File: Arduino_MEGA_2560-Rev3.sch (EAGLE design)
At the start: 63 parts, among them IC1 NCP1117ST50T3G, IC3 ATMEGA2560-16AU, IC4 ATMEGA16U2-MU, IC6 LP2985-33DBVR, IC7 LMV358IDGKR, T1 FDN340P, X1 POWERSUPPLY_DC21MMX, X2 USB-B_TH, Y1 CSTCE16M0V53-R0 16MHZ, Y2 16MHz

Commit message: Version inicial del Shield
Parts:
- removed C1, C14, C15: 22p, SmartPrj:C-EU0603-RND
- removed C10, C13: 1u, SmartPrj:C-EU0603-RND
- removed C11, C12, C2, C3, C4, C5, C6, C7, C8, C9: 100n, SmartPrj:C-EU0603-RND
- removed D1: M7, diode:DIODE-SMB
- removed D2, D3: CD1206-S01575, diode:DIODE-MINIMELF
- removed F1: MF-MSMF050-2 500mA, rcl:L-EUL1812
- removed FD1, FD2, FD3, FD4: FIDUCIALMOUNT, SmartPrj:FIDUCIALMOUNT
- removed GROUND, RESET-EN: (no value), jumper:SJ
- removed IC1: NCP1117ST50T3G, linear:MC33269ST-3.3T3
- removed IC3: ATMEGA2560-16AU, SmartPrj:ATMEGA25602560-16AU
- removed IC4: ATMEGA16U2-MU, SmartPrj:ATMEGA16U2-MU
- removed IC6: LP2985-33DBVR, SmartPrj:LP2985-XXDBVR33
- removed IC7: LMV358IDGKR, linear:LMV358MMX
- removed ICSP, ICSP1: 3x2M, SmartPrj:PINHD-2X3
- removed JP5: 2x2M - NM, SmartPrj:PINHD-2X2
- removed L, RX, TX: YELLOW, led:LEDCHIP-LED0805
- removed L1: BLM21, wuerth-elektronik:WE-CBF_0805
- removed ON: GREEN, led:LEDCHIP-LED0805
- removed PC1, PC2: 47u, rcl:CPOL-EUD
- removed RESET: TS42031-160R-TR-7260, SmartPrj:TS42
- removed RN1, RN5: 10K, resistor-dil:4R-NCAT16
- removed RN2: 22R, resistor-dil:4R-NCAY16
- removed RN3, RN4: 1k, resistor-dil:4R-NCAY16
- removed T1: FDN340P, zetex:PMOSSOT23
- removed X1: POWERSUPPLY_DC21MMX, SmartPrj:POWERSUPPLY_DC21MMX
- removed X2: USB-B_TH, SmartPrj:PN61729
- removed Y1: CSTCE16M0V53-R0 16MHZ, SmartPrj:RESONATORMU
- removed Y2: 16MHz, SmartPrj:XTAL/S
- removed Z1, Z2: CG0603MLC-05E, varistor:VARISTORCN0603
- added LED1, LED2: (no value), led:LEDCHIPLED_1206
- added R10, R11, R12, R13, R14, R15, R16, R17, R18, R19, R20, R3, R4, R5, R6, R7, R8, R9: (no value), resistor:R-EU_M1206
- added U$2, U$3, U$4, U$5, U$6, U$7, U$8, U$9: XPORT, SparkFun-Boards:XPORT
- R1, R2: value 1M -> (none); device SmartPrj:R-EU_R0603 -> resistor:R-EU_M1206
- U$1: value DISCLAIMER -> XPORT; device SmartPrj:DISCLAIMER -> SparkFun-Boards:XPORT
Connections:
- removed net 8PB4: IC4.(T1/PCINT4)PB4, JP5.1
- removed net 8PB5: IC4.(PCINT5)PB5, JP5.3
- removed net 8PB6: IC4.(PCINT6)PB6, JP5.2
- removed net 8PB7: IC4.(PCINT7/OC0A/OC1C)PB7, JP5.4
- removed net ADC0: ADCL.1, IC3.(ADC0)PF0
- removed net ADC1: ADCL.2, IC3.(ADC1)PF1
- removed net ADC10: ADCH.3, IC3.PK2(ADC10/PCINT18)
- removed net ADC11: ADCH.4, IC3.PK3(ADC11/PCINT19)
- removed net ADC12: ADCH.5, IC3.PK4(ADC12/PCINT20)
- removed net ADC13: ADCH.6, IC3.PK5(ADC13/PCINT21)
- removed net ADC14: ADCH.7, IC3.PK6(ADC14/PCINT22)
- removed net ADC15: ADCH.8, IC3.PK7(ADC15/PCINT23)
- removed net ADC2: ADCL.3, IC3.(ADC2)PF2
- removed net ADC3: ADCL.4, IC3.(ADC3)PF3
- removed net ADC4: ADCL.5, IC3.(ADC4/TCK)PF4
- removed net ADC5: ADCL.6, IC3.(ADC5/TMS)PF5
- removed net ADC6: ADCL.7, IC3.(ADC6/TDO)PF6
- removed net ADC7: ADCL.8, IC3.(ADC7/TDI)PF7
- removed net ADC8: ADCH.1, IC3.PK0(ADC8/PCINT16)
- removed net ADC9: ADCH.2, IC3.PK1(ADC9/PCINT17)
- removed net CMP: C12.2, IC7B.+IN, RN5C.1, RN5D.2
- removed net D+: RN2D.2, X2.3, Z2.2
- removed net D-: RN2A.2, X2.2, Z1.2
- removed net DTR: C7.1, IC4.(CTS/HWB/AIN6/TO/INT7)PD7, RN3D.1
- removed net GATE_CMD: IC7B.OUT, T1.G
- removed net L13: IC7A.-IN, IC7A.OUT, RN3B.2
- removed net M8RXD: IC4.(TXD1/INT3)PD3, RN4B.2
- removed net M8TXD: IC4.(RXD1/AIN1/INT2)PD2, RN4A.2
- removed net MISO2: IC4.(PD0/MISO/PCINT3)PB3, ICSP1.1
- removed net MOSI2: IC4.(PDI/MOSI/PCINT2)PB2, ICSP1.4
- removed net N$54: RN4D.1, RX.A
- removed net N$55: RN4C.1, TX.A
- removed net PWRIN: D1.A, X1.2
- removed net RD+: IC4.D+, RN2D.1
- removed net RD-: IC4.D-, RN2A.1
- removed net RESET2: D2.A, IC4.RESET(PC1/DW), ICSP1.5, RN5B.2
- removed net RXL: IC4.(INT5/AIN3)PD4, RX.C
- removed net SCK2: IC4.(SCLK/PCINT1)PB1, ICSP1.3
- removed net TXL: IC4.(XCK/AIN4/PCINT12)PD5, TX.C
- removed net UGND: C10.2, GROUND.1, IC4.UGND, L1.1, X2.4
- removed net USBVCC: C8.1, F1.1, IC4.UVCC, T1.D
- removed net USHIELD: L1.2, X2.P$1, X2.P$2, Z1.1, Z2.1
- removed net VUCAP: C10.1, IC4.UCAP
- removed net XT1: C14.1, IC4.XTAL1, R2.1, Y2.2
- removed net XT2: C15.1, IC4.XTAL2(PC0), R2.2, Y2.1
- removed net XTAL1: IC3.XTAL1, R1.1, Y1.3
- removed net XTAL2: IC3.XTAL2, R1.2, Y1.1
- removed net XVCC: F1.2, X2.1
- new net N$1: LED1.A, R1.1
- new net N$10: ADCH.3, R7.2
- new net N$11: ADCL.4, R14.2
- new net N$12: ADCL.5, R15.2
- new net N$13: ADCL.6, R16.2
- new net N$14: ADCL.7, R17.2
- new net N$15: ADCL.8, R18.2
- new net N$16: R12.1, U$8.DTR
- new net N$17: R13.1, U$8.RTS
- new net N$18: R14.1, U$8.RX
- new net N$19: R15.1, U$8.TX
- new net N$20: R16.1, U$8.RST
- new net N$21: ADCH.4, R8.2
- new net N$22: ADCH.5, R9.2
- new net N$23: ADCH.6, R10.2
- new net N$24: ADCH.7, R4.2
- new net N$25: ADCH.8, R3.2
- new net N$26: R17.1, U$2.CTS
- new net N$27: R18.1, U$2.DTR
- new net N$28: R5.1, U$2.RTS
- new net N$29: R6.1, U$2.RX
- new net N$30: R7.1, U$2.TX
- new net N$31: R8.1, U$2.RST
- new net N$32: R9.1, U$3.CTS
- new net N$33: R10.1, U$3.DTR
- new net N$34: R4.1, U$3.RTS
- new net N$35: R3.1, U$3.RX
- new net N$36: R19.1, U$3.RST
- new net N$37: R20.2, XIO.33
- new net N$4: ADCH.2, R6.2
- new net N$5: JP6.2
- new net N$6: R11.1, U$8.CTS
- new net N$7: ADCL.1, R11.2
- new net N$8: ADCL.2, R12.2
- new net N$9: ADCL.3, R13.2
- net +3V3: no longer C13.2, IC6.OUT, IC7B.-IN
- net +5V: now also R1.2, R2.2; no longer C11.2, C4.1, C5.1, C6.1, C9.1, D2.C, D3.C, IC1.OUT, IC1.OUT@1, IC3.AVCC, IC3.VCC, IC3.VCC1, IC3.VCC2, IC3.VCC3, IC4.AVCC, IC4.VCC, IC6.IN, IC6.ON/!OFF, IC7P.V+, ICSP.2, ICSP1.2, PC2.+, RN1B.2, RN1C.2, RN3A.1, RN4C.2, RN4D.2, RN5A.2, RN5B.1, T1.S
- net AREF: no longer C3.1, IC3.AREF
- net GND: now also LED1.C, LED2.C, U$1.3.3V, U$1.GND, U$2.3.3V, U$2.GND, U$3.3.3V, U$3.GND, U$4.3.3V, U$4.GND, U$5.3.3V, U$5.GND, U$6.3.3V, U$6.GND, U$7.3.3V, U$7.GND, U$8.3.3V, U$8.GND, U$9.3.3V, U$9.GND; no longer C1.2, C11.1, C12.1, C13.1, C14.2, C15.2, C2.2, C3.2, C4.2, C5.2, C6.2, C8.2, C9.2, GROUND.2, IC1.GND/ADJ, IC3.AGND, IC3.GND, IC3.GND1, IC3.GND2, IC3.GND3, IC4.GND, IC4.PAD, IC6.GND, IC7P.V-, ICSP.6, ICSP1.6, L.C, ON.C, PC1.-, PC2.-, RESET.1, RESET.2, RN3D.2, RN5D.1, X1.1, X1.3, Y1.2
- net N$2: now also LED2.A, R2.1; no longer L.A, RN3B.1
- net N$3: now also ADCH.1, R5.2; no longer ON.A, RN3A.2
- net PA0: no longer IC3.(AD0)PA0
- net PA1: no longer IC3.(AD1)PA1
- net PA2: no longer IC3.(AD2)PA2
- net PA3: no longer IC3.(AD3)PA3
- net PA4: no longer IC3.(AD4)PA4
- net PA5: no longer IC3.(AD5)PA5
- net PA6: no longer IC3.(AD6)PA6
- net PA7: no longer IC3.(AD7)PA7
- net PB0: now also R19.2; no longer IC3.(SS/PCINT0)PB0
- net PB1: now also R20.1, U$3.TX; no longer IC3.(SCK/PCINT1)PB1, ICSP.3, XIO.33
- net PB2: no longer IC3.(MOSI/PCINT2)PB2, ICSP.4
- net PB3: no longer IC3.(MISO/PCINT3)PB3, ICSP.1
- net PB4: no longer IC3.(OC2A/PCINT4)PB4
- net PB5: no longer IC3.(OC1A/PCINT5)PB5
- net PB6: no longer IC3.(OC1B/PCINT6)PB6
- net PB7: no longer IC3.(OC0A/OC1C/PCINT7)PB7, IC7A.+IN
- net PC0: no longer IC3.(A8)PC0
- net PC1: no longer IC3.(A9)PC1
- net PC2: no longer IC3.(A10)PC2
- net PC3: no longer IC3.(A11)PC3
- net PC4: no longer IC3.(A12)PC4
- net PC5: no longer IC3.(A13)PC5
- net PC6: no longer IC3.(A14)PC6
- net PC7: no longer IC3.(A15)PC7
- net PD7: no longer IC3.(T0)PD7
- net PE0: no longer IC3.(RXD0/PCIN8)PE0, RN4B.1
- net PE1: no longer IC3.(TXD0)PE1, RN4A.1
- net PE3: no longer IC3.(OC3A/AIN1)PE3
- net PE4: no longer IC3.(OC3B/INT4)PE4
- net PE5: no longer IC3.(OC3C/INT5)PE5
- net PG0: no longer IC3.(WR)PG0
- net PG1: no longer IC3.(RD)PG1
- net PG2: no longer IC3.(ALE)PG2
- net PG5: no longer IC3.(OC0B)PG5
- net PH3: no longer IC3.PH3(OC4A)
- net PH4: no longer IC3.PH4(OC4B)
- net PH5: no longer IC3.PH5(OC4C)
- net PH6: no longer IC3.PH6(OC2B)
- net PL0: no longer IC3.PL0(ICP4)
- net PL1: no longer IC3.PL1(ICP5)
- net PL2: no longer IC3.PL2(T5)
- net PL3: no longer IC3.PL3(OC5A)
- net PL4: no longer IC3.PL4(OC5B)
- net PL5: no longer IC3.PL5(OC5C)
- net PL6: no longer IC3.PL6
- net PL7: no longer IC3.PL7
- net RESET: no longer C1.1, C7.2, D3.A, IC3.RESET, ICSP.5, RESET-EN.1, RESET-EN.2, RESET.3, RESET.4, RN5A.1
- net RXD1: no longer IC3.(RXD1/INT2)PD2
- net RXD2: no longer IC3.PH0(RXD2)
- net RXD3: no longer IC3.PJ0(RXD3/PCINT9)
- net SCL: no longer IC3.(SCL/INT0)PD0, RN1B.1
- net SDA: no longer IC3.(SDA/INT1)PD1, JP6.2, RN1C.1
- net TXD1: no longer IC3.(TXD1/INT3)PD3
- net TXD2: no longer IC3.PH1(TXD2)
- net TXD3: no longer IC3.PJ1(TXD3/PCINT10)
- net VIN: no longer C2.1, D1.C, IC1.IN, PC1.+, RN5C.2
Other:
- note removed: "USB boot En"
- moved on the sheet: ADCH, ADCL, COMMUNICATION, JP6, PWML, R1, R2, XIO

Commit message: nuevas dimensiones placa
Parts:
- removed R10, R16, R17, R18, R4, R5, R6, R9: (no value), resistor:R-EU_M1206
- added R21, R25: (no value), rcl:R-US_0207/2V
- R11, R12, R13, R14, R15, R19, R20, R3, R7, R8: device resistor:R-EU_M1206 -> rcl:R-US_0207/10
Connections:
- removed net N$18: R14.1, U$8.RX
- removed net N$19: R15.1, U$8.TX
- removed net N$20: R16.1, U$8.RST
- removed net N$26: R17.1, U$2.CTS
- removed net N$27: R18.1, U$2.DTR
- removed net N$28: R5.1, U$2.RTS
- removed net N$29: R6.1, U$2.RX
- removed net N$32: R9.1, U$3.CTS
- removed net N$33: R10.1, U$3.DTR
- removed net N$34: R4.1, U$3.RTS
- removed net N$35: R3.1, U$3.RX
- new net N$38: R21.2, U$7.TX
- new net N$39: R25.1, U$7.RST
- new net N$44: R11.1, U$8.RST
- new net N$45: R12.1, U$8.TX
- new net N$46: R13.2, U$8.3.3V, U$8.GND
- net GND: now also R13.1, R14.2, R15.1, R3.2; no longer U$2.3.3V, U$2.GND, U$3.3.3V, U$3.GND, U$7.3.3V, U$7.GND, U$8.3.3V, U$8.GND
- net N$11: now also U$8.RX; no longer R14.2
- net N$12: now also R12.2; no longer R15.2
- net N$13: now also R11.2; no longer R16.2
- net N$14: now also U$2.CTS; no longer R17.2
- net N$15: now also U$2.DTR; no longer R18.2
- net N$16: now also R15.2, U$2.3.3V, U$2.GND; no longer R12.1, U$8.DTR
- net N$17: now also R3.1, U$3.3.3V, U$3.GND; no longer R13.1, U$8.RTS
- net N$22: now also U$3.CTS; no longer R9.2
- net N$23: now also U$3.DTR; no longer R10.2
- net N$24: now also U$3.RTS; no longer R4.2
- net N$25: now also U$3.RX; no longer R3.2
- net N$3: now also U$2.RTS; no longer R5.2
- net N$4: now also U$2.RX; no longer R6.2
- net N$6: now also R14.1, U$7.3.3V, U$7.GND; no longer R11.1, U$8.CTS
- net N$7: now also U$8.CTS; no longer R11.2
- net N$8: now also U$8.DTR; no longer R12.2
- net N$9: now also U$8.RTS; no longer R13.2
- net PB2: now also U$1.DTR
- net PB3: now also U$1.CTS
- net PB4: now also U$7.CTS
- net PB5: now also R21.1
- net PB6: now also R25.2
- net PB7: now also U$7.RX
- net PG0: now also U$9.RST
- net PG1: now also U$9.TX
- net PH5: now also U$7.DTR
- net PH6: now also U$7.RTS
- net PL0: now also U$1.RX
- net PL1: now also U$1.RTS
- net PL2: now also U$1.RST
- net PL3: now also U$1.TX
- net PL4: now also U$9.DTR
- net PL5: now also U$9.CTS
- net PL6: now also U$9.RX
- net PL7: now also U$9.RTS
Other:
- moved on the sheet: U$1, U$4, U$5, U$6, U$7, U$9

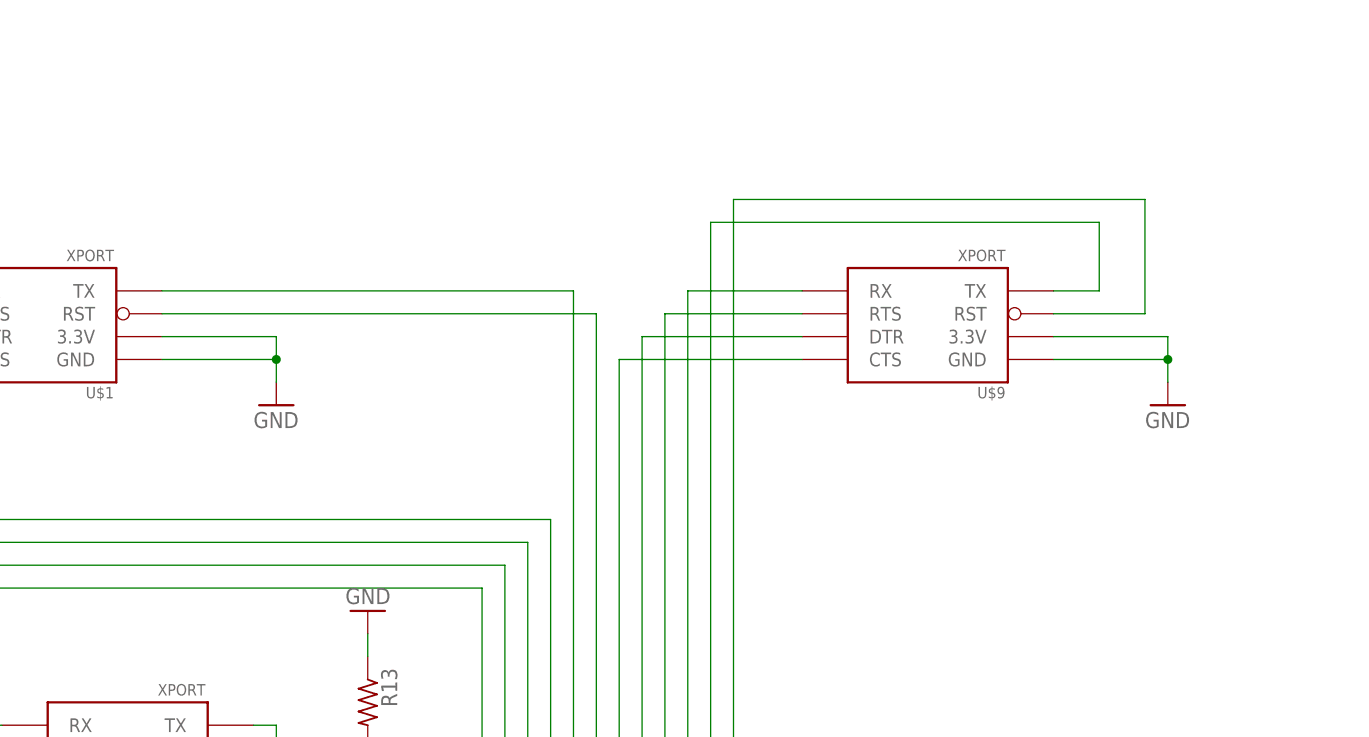
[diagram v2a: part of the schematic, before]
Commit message: nuevas resistencias, revisar los pines de entrada salida
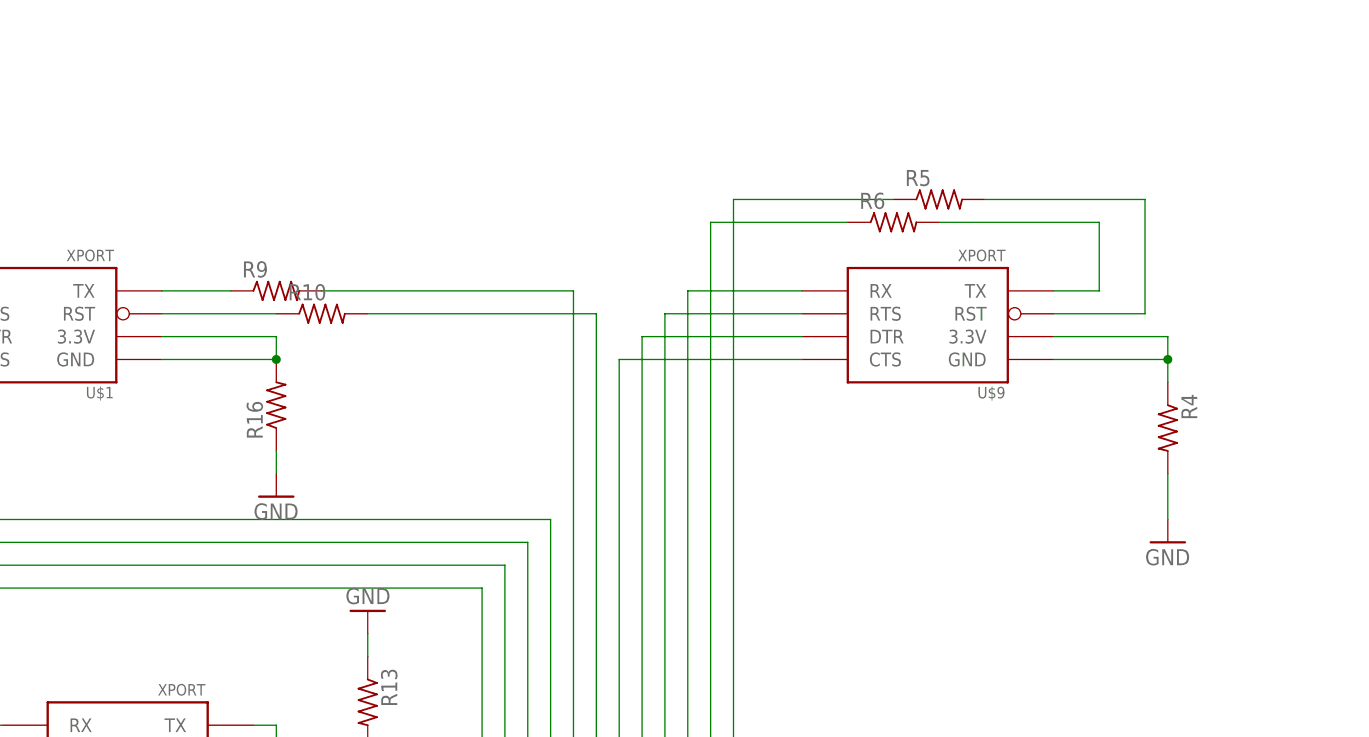
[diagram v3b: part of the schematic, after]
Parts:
- added R10, R16, R4, R5, R6, R9: (no value), rcl:R-US_0207/15
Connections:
- new net N$18: R4.1, U$9.3.3V, U$9.GND
- new net N$19: R5.2, U$9.RST
- new net N$20: R6.2, U$9.TX
- new net N$26: R16.2, U$1.3.3V, U$1.GND
- new net N$27: R10.1, U$1.RST
- new net N$28: R9.1, U$1.TX
- net GND: now also R16.1, R4.2; no longer U$1.3.3V, U$1.GND, U$9.3.3V, U$9.GND
- net PG0: now also R5.1; no longer U$9.RST
- net PG1: now also R6.1; no longer U$9.TX
- net PL2: now also R10.2; no longer U$1.RST
- net PL3: now also R9.2; no longer U$1.TX
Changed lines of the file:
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@@
 <part name="R15" library="rcl" deviceset="R-US_" device="0207/10"/>
 <part name="R3" library="rcl" deviceset="R-US_" device="0207/10"/>
+<part name="R4" library="rcl" deviceset="R-US_" device="0207/15"/>
+<part name="R5" library="rcl" deviceset="R-US_" device="0207/15"/>
+<part name="R6" library="rcl" deviceset="R-US_" device="0207/15"/>
+<part name="R9" library="rcl" deviceset="R-US_" device="0207/15"/>
+<part name="R10" library="rcl" deviceset="R-US_" device="0207/15"/>
+<part name="R16" library="rcl" deviceset="R-US_" device="0207/15"/>
 </parts>
 <sheets>
@@
 <attribute name="VALUE" x="230.886" y="146.812" size="1.27" layer="96" rot="R180"/>
 </instance>
-<instance part="GND1" gate="1" x="149.86" y="129.54" smashed="yes">
-<attribute name="VALUE" x="147.32" y="127" size="1.778" layer="96"/>
+<instance part="GND1" gate="1" x="149.86" y="119.38" smashed="yes">
+<attribute name="VALUE" x="147.32" y="116.84" size="1.778" layer="96"/>
 </instance>
 <instance part="GND2" gate="1" x="350.52" y="185.42" smashed="yes" rot="R180">
@@
 <attribute name="VALUE" x="162.56" y="109.22" size="1.778" layer="96" rot="R180"/>
 </instance>
-<instance part="GND14" gate="1" x="248.92" y="129.54" smashed="yes">
-<attribute name="VALUE" x="246.38" y="127" size="1.778" layer="96"/>
+<instance part="GND14" gate="1" x="248.92" y="114.3" smashed="yes">
+<attribute name="VALUE" x="246.38" y="111.76" size="1.778" layer="96"/>
 </instance>
 <instance part="R7" gate="G$1" x="83.82" y="50.8" smashed="yes" rot="R180">
@@
 <attribute name="NAME" x="151.3586" y="29.21" size="1.778" layer="95" rot="R270"/>
 <attribute name="VALUE" x="146.558" y="29.21" size="1.778" layer="96" rot="R270"/>
+</instance>
+<instance part="R4" gate="G$1" x="248.92" y="127" smashed="yes" rot="R270">
+<attribute name="NAME" x="250.4186" y="130.81" size="1.778" layer="95" rot="R270"/>
+<attribute name="VALUE" x="245.618" y="130.81" size="1.778" layer="96" rot="R270"/>
+</instance>
+<instance part="R5" gate="G$1" x="223.52" y="152.4" smashed="yes">
+<attribute name="NAME" x="219.71" y="153.8986" size="1.778" layer="95"/>
+<attribute name="VALUE" x="219.71" y="149.098" size="1.778" layer="96"/>
+</instance>
+<instance part="R6" gate="G$1" x="218.44" y="149.86" smashed="yes">
+<attribute name="NAME" x="214.63" y="151.3586" size="1.778" layer="95"/>
+<attribute name="VALUE" x="214.63" y="146.558" size="1.778" layer="96"/>
+</instance>
+<instance part="R9" gate="G$1" x="149.86" y="142.24" smashed="yes">
+<attribute name="NAME" x="146.05" y="143.7386" size="1.778" layer="95"/>
+<attribute name="VALUE" x="146.05" y="138.938" size="1.778" layer="96"/>
+</instance>
+<instance part="R10" gate="G$1" x="154.94" y="139.7" smashed="yes">
+<attribute name="NAME" x="151.13" y="141.1986" size="1.778" layer="95"/>
+<attribute name="VALUE" x="151.13" y="136.398" size="1.778" layer="96"/>
+</instance>
+<instance part="R16" gate="G$1" x="149.86" y="129.54" smashed="yes" rot="R90">
+<attribute name="NAME" x="148.3614" y="125.73" size="1.778" layer="95" rot="R90"/>
+<attribute name="VALUE" x="153.162" y="125.73" size="1.778" layer="96" rot="R90"/>
 </instance>
 </instances>
@@
 </segment>
 <segment>
-<pinref part="GND1" gate="1" pin="GND"/>
-<pinref part="U$1" gate="G$1" pin="GND"/>
-<wire x1="137.16" y1="134.62" x2="149.86" y2="134.62" width="0.1524" layer="91"/>
-<wire x1="149.86" y1="134.62" x2="149.86" y2="132.08" width="0.1524" layer="91"/>
-<junction x="149.86" y="134.62"/>
-<wire x1="149.86" y1="137.16" x2="149.86" y2="134.62" width="0.1524" layer="91"/>
-<pinref part="U$1" gate="G$1" pin="3.3V"/>
-<wire x1="137.16" y1="137.16" x2="149.86" y2="137.16" width="0.1524" layer="91"/>
-</segment>
-<segment>
 <pinref part="LED1" gate="G$1" pin="C"/>
 <pinref part="GND3" gate="1" pin="GND"/>
@@
 </segment>
 <segment>
-<pinref part="U$9" gate="G$1" pin="GND"/>
-<wire x1="236.22" y1="134.62" x2="248.92" y2="134.62" width="0.1524" layer="91"/>
-<pinref part="U$9" gate="G$1" pin="3.3V"/>
-<wire x1="236.22" y1="137.16" x2="248.92" y2="137.16" width="0.1524" layer="91"/>
-<wire x1="248.92" y1="137.16" x2="248.92" y2="134.62" width="0.1524" layer="91"/>
-<pinref part="GND14" gate="1" pin="GND"/>
-<wire x1="248.92" y1="132.08" x2="248.92" y2="134.62" width="0.1524" layer="91"/>
-<junction x="248.92" y="134.62"/>
-</segment>
-<segment>
 <pinref part="U$6" gate="G$1" pin="GND"/>
 <wire x1="495.3" y1="152.4" x2="482.6" y2="152.4" width="0.1524" layer="91"/>
@@
 <pinref part="GND7" gate="1" pin="GND"/>
 <wire x1="149.86" y1="20.32" x2="149.86" y2="17.78" width="0.1524" layer="91"/>
+</segment>
+<segment>
+<pinref part="R4" gate="G$1" pin="2"/>
+<pinref part="GND14" gate="1" pin="GND"/>
+<wire x1="248.92" y1="121.92" x2="248.92" y2="116.84" width="0.1524" layer="91"/>
+</segment>
+<segment>
+<pinref part="GND1" gate="1" pin="GND"/>
+<pinref part="R16" gate="G$1" pin="1"/>
+<wire x1="149.86" y1="121.92" x2="149.86" y2="124.46" width="0.1524" layer="91"/>
 </segment>
 </net>
@@
 <wire x1="248.92" y1="58.42" x2="200.66" y2="58.42" width="0.1524" layer="91"/>
 <wire x1="200.66" y1="58.42" x2="200.66" y2="152.4" width="0.1524" layer="91"/>
-<wire x1="200.66" y1="152.4" x2="246.38" y2="152.4" width="0.1524" layer="91"/>
-<wire x1="246.38" y1="152.4" x2="246.38" y2="139.7" width="0.1524" layer="91"/>
-<pinref part="U$9" gate="G$1" pin="RST"/>
-<wire x1="246.38" y1="139.7" x2="236.22" y2="139.7" width="0.1524" layer="91"/>
+<pinref part="R5" gate="G$1" pin="1"/>
+<wire x1="200.66" y1="152.4" x2="218.44" y2="152.4" width="0.1524" layer="91"/>
 </segment>
 <segment>
@@
 <wire x1="185.42" y1="55.88" x2="198.12" y2="55.88" width="0.1524" layer="91"/>
 <wire x1="198.12" y1="55.88" x2="198.12" y2="149.86" width="0.1524" layer="91"/>
-<wire x1="198.12" y1="149.86" x2="241.3" y2="149.86" width="0.1524" layer="91"/>
-<wire x1="241.3" y1="149.86" x2="241.3" y2="142.24" width="0.1524" layer="91"/>
-<pinref part="U$9" gate="G$1" pin="TX"/>
-<wire x1="241.3" y1="142.24" x2="236.22" y2="142.24" width="0.1524" layer="91"/>
+<pinref part="R6" gate="G$1" pin="1"/>
+<wire x1="198.12" y1="149.86" x2="213.36" y2="149.86" width="0.1524" layer="91"/>
 </segment>
 <segment>
@@
 <wire x1="256.54" y1="71.12" x2="185.42" y2="71.12" width="0.1524" layer="91"/>
 <wire x1="185.42" y1="71.12" x2="185.42" y2="139.7" width="0.1524" layer="91"/>
-<pinref part="U$1" gate="G$1" pin="RST"/>
-<wire x1="185.42" y1="139.7" x2="137.16" y2="139.7" width="0.1524" layer="91"/>
+<pinref part="R10" gate="G$1" pin="2"/>
+<wire x1="160.02" y1="139.7" x2="185.42" y2="139.7" width="0.1524" layer="91"/>
 </segment>
 </net>
@@
 <wire x1="177.8" y1="63.5" x2="182.88" y2="63.5" width="0.1524" layer="91"/>
 <wire x1="182.88" y1="63.5" x2="182.88" y2="142.24" width="0.1524" layer="91"/>
-<pinref part="U$1" gate="G$1" pin="TX"/>
-<wire x1="182.88" y1="142.24" x2="137.16" y2="142.24" width="0.1524" layer="91"/>
+<pinref part="R9" gate="G$1" pin="2"/>
+<wire x1="154.94" y1="142.24" x2="182.88" y2="142.24" width="0.1524" layer="91"/>
 </segment>
 </net>
@@
 </segment>
 </net>
+<net name="N$18" class="2">
+<segment>
+<pinref part="U$9" gate="G$1" pin="GND"/>
+<wire x1="236.22" y1="134.62" x2="248.92" y2="134.62" width="0.1524" layer="91"/>
+<pinref part="U$9" gate="G$1" pin="3.3V"/>
+<wire x1="236.22" y1="137.16" x2="248.92" y2="137.16" width="0.1524" layer="91"/>
+<wire x1="248.92" y1="137.16" x2="248.92" y2="134.62" width="0.1524" layer="91"/>
+<pinref part="R4" gate="G$1" pin="1"/>
+<wire x1="248.92" y1="132.08" x2="248.92" y2="134.62" width="0.1524" layer="91"/>
+<junction x="248.92" y="134.62"/>
+</segment>
+</net>
+<net name="N$19" class="0">
+<segment>
+<pinref part="U$9" gate="G$1" pin="RST"/>
+<wire x1="246.38" y1="152.4" x2="246.38" y2="139.7" width="0.1524" layer="91"/>
+<wire x1="246.38" y1="139.7" x2="236.22" y2="139.7" width="0.1524" layer="91"/>
+<pinref part="R5" gate="G$1" pin="2"/>
+<wire x1="228.6" y1="152.4" x2="246.38" y2="152.4" width="0.1524" layer="91"/>
+</segment>
+</net>
+<net name="N$20" class="0">
+<segment>
+<pinref part="U$9" gate="G$1" pin="TX"/>
+<wire x1="241.3" y1="149.86" x2="241.3" y2="142.24" width="0.1524" layer="91"/>
+<wire x1="241.3" y1="142.24" x2="236.22" y2="142.24" width="0.1524" layer="91"/>
+<pinref part="R6" gate="G$1" pin="2"/>
+<wire x1="223.52" y1="149.86" x2="241.3" y2="149.86" width="0.1524" layer="91"/>
+</segment>
+</net>
+<net name="N$26" class="2">
+<segment>
+<pinref part="U$1" gate="G$1" pin="GND"/>
+<wire x1="137.16" y1="134.62" x2="149.86" y2="134.62" width="0.1524" layer="91"/>
+<wire x1="149.86" y1="137.16" x2="149.86" y2="134.62" width="0.1524" layer="91"/>
+<pinref part="U$1" gate="G$1" pin="3.3V"/>
+<wire x1="137.16" y1="137.16" x2="149.86" y2="137.16" width="0.1524" layer="91"/>
+<pinref part="R16" gate="G$1" pin="2"/>
+<junction x="149.86" y="134.62"/>
+</segment>
+</net>
+<net name="N$27" class="0">
+<segment>
+<pinref part="U$1" gate="G$1" pin="RST"/>
+<pinref part="R10" gate="G$1" pin="1"/>
+<wire x1="137.16" y1="139.7" x2="149.86" y2="139.7" width="0.1524" layer="91"/>
+</segment>
+</net>
+<net name="N$28" class="0">
+<segment>
+<pinref part="U$1" gate="G$1" pin="TX"/>
+<pinref part="R9" gate="G$1" pin="1"/>
+<wire x1="137.16" y1="142.24" x2="144.78" y2="142.24" width="0.1524" layer="91"/>
+</segment>
+</net>
